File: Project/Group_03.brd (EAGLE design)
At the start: 56.4 x 71.1 mm, 29 parts, among them J1 POWER_JACKPTH_LOCK, U1 +12v, U3 TCA9546APW, U4 TMUX1208RSV

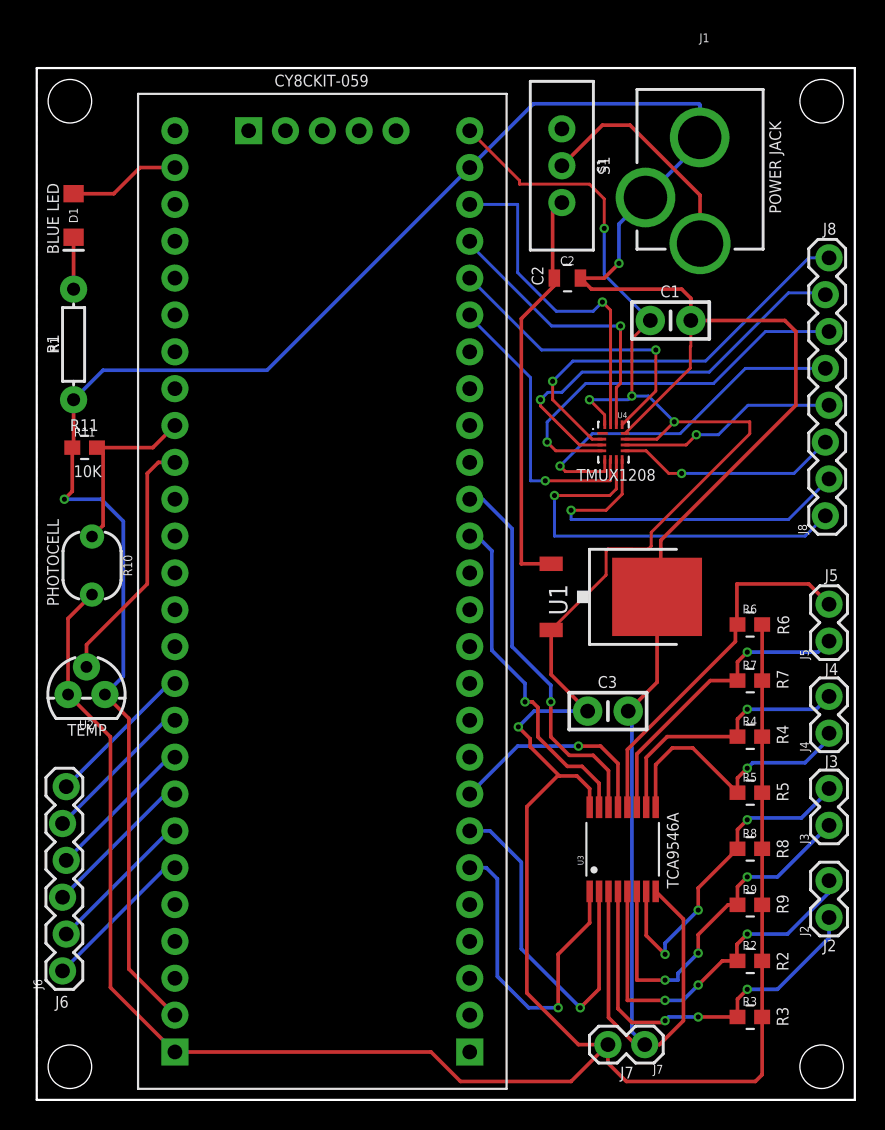
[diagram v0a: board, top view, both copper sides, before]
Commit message: Polygon isolation correction
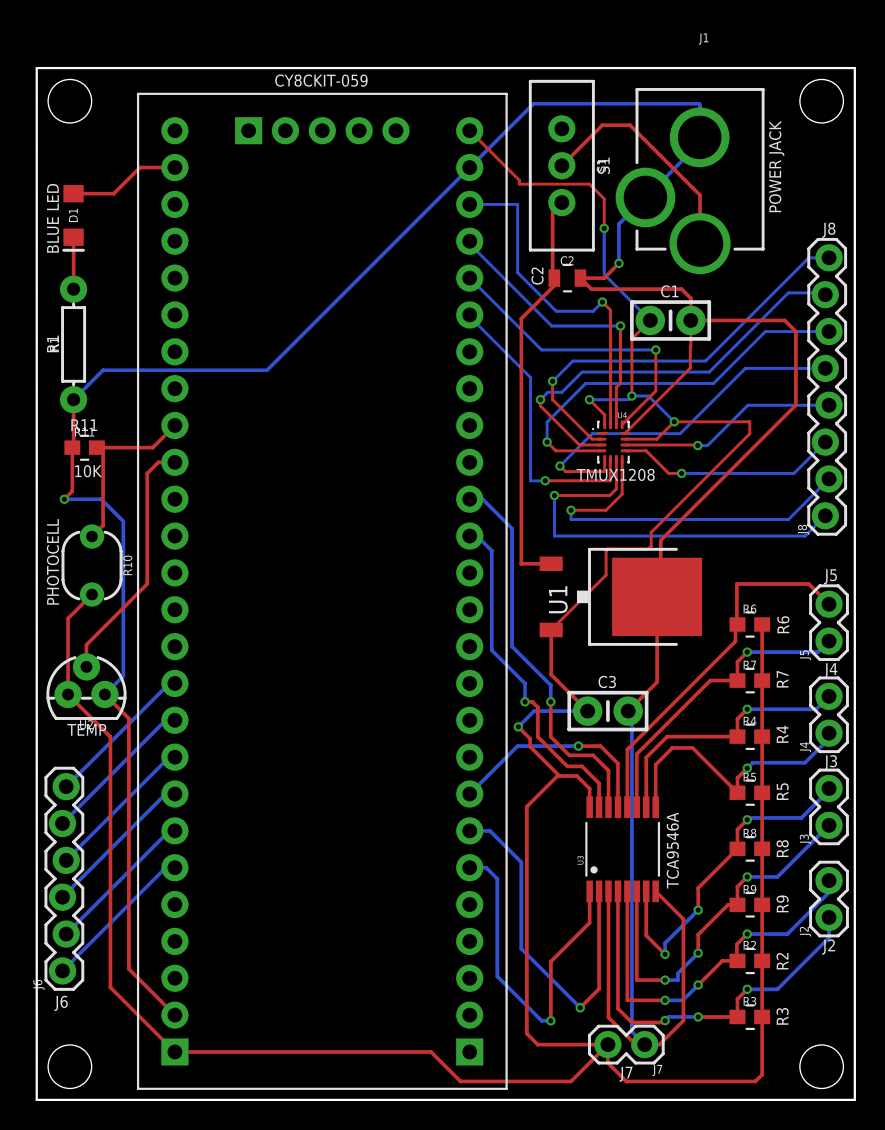
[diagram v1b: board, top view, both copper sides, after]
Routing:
- net 5V: track 220.2 -> 221.8 mm
- net I2C_A0: track 23.0 -> 23.9 mm
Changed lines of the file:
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@@
 <layer number="27" name="tValues" color="7" fill="1" visible="yes" active="yes"/>
 <layer number="28" name="bValues" color="7" fill="1" visible="yes" active="yes"/>
-<layer number="29" name="tStop" color="7" fill="3" visible="yes" active="yes"/>
+<layer number="29" name="tStop" color="7" fill="3" visible="no" active="yes"/>
 <layer number="30" name="bStop" color="7" fill="6" visible="no" active="yes"/>
 <layer number="31" name="tCream" color="7" fill="4" visible="no" active="yes"/>
@@
 <layer number="35" name="tGlue" color="7" fill="4" visible="no" active="yes"/>
 <layer number="36" name="bGlue" color="7" fill="5" visible="no" active="yes"/>
-<layer number="37" name="tTest" color="7" fill="1" visible="yes" active="yes"/>
-<layer number="38" name="bTest" color="7" fill="1" visible="yes" active="yes"/>
+<layer number="37" name="tTest" color="7" fill="1" visible="no" active="yes"/>
+<layer number="38" name="bTest" color="7" fill="1" visible="no" active="yes"/>
 <layer number="39" name="tKeepout" color="4" fill="11" visible="no" active="yes"/>
 <layer number="40" name="bKeepout" color="1" fill="11" visible="no" active="yes"/>
@@
 <layer number="49" name="Reference" color="7" fill="1" visible="yes" active="yes"/>
 <layer number="50" name="dxf" color="7" fill="1" visible="no" active="no"/>
-<layer number="51" name="tDocu" color="7" fill="1" visible="no" active="yes"/>
+<layer number="51" name="tDocu" color="7" fill="1" visible="yes" active="yes"/>
 <layer number="52" name="bDocu" color="7" fill="1" visible="yes" active="yes"/>
 <layer number="53" name="tGND_GNDA" color="7" fill="9" visible="no" active="no"/>
@@
 <text x="16.383" y="69.85" size="0.8128" layer="21" font="vector" ratio="24">CY8CKIT-059</text>
 <wire x1="3.048" y1="45.77" x2="3.556" y2="45.77" width="0.1524" layer="21"/>
-<wire x1="3.048" y1="44.173" x2="3.556" y2="44.173" width="0.1524" layer="21"/>
+<wire x1="3.048" y1="44.123" x2="3.556" y2="44.123" width="0.1524" layer="21"/>
 <wire x1="48.895" y1="33.601" x2="49.403" y2="33.601" width="0.1524" layer="21"/>
 <wire x1="48.915" y1="31.931" x2="49.423" y2="31.931" width="0.1524" layer="21"/>
@@
 <wire x1="34.0106" y1="24.8904" x2="33.193" y2="25.708" width="0.254" layer="1"/>
 <wire x1="38.111" y1="21.452" x2="37.2364" y2="22.3266" width="0.254" layer="1"/>
-<wire x1="39.37" y1="3.81" x2="37.338" y2="3.81" width="0.254" layer="1"/>
-<wire x1="37.338" y1="3.81" x2="33.782" y2="7.366" width="0.254" layer="1"/>
-<wire x1="33.782" y1="7.366" x2="33.782" y2="20.2089375" width="0.254" layer="1"/>
+<wire x1="39.37" y1="3.81" x2="34.538" y2="3.81" width="0.254" layer="1"/>
+<wire x1="34.538" y1="3.81" x2="33.782" y2="4.566" width="0.254" layer="1"/>
+<wire x1="33.782" y1="4.566" x2="33.782" y2="20.2089375" width="0.254" layer="1"/>
 <wire x1="33.782" y1="20.2089375" x2="35.8996625" y2="22.3266" width="0.254" layer="1"/>
 <wire x1="49.999" y1="32.765996875" x2="49.999" y2="28.90156875" width="0.254" layer="1"/>
@@
 <wire x1="37.973" y1="26.797" x2="35.459" y2="29.311" width="0.254" layer="1"/>
 <wire x1="39.243" y1="36.175" x2="35.459" y2="32.391" width="0.2032" layer="1"/>
-<polygon width="0.1524" layer="16" isolate="0.254">
+<polygon width="0.1524" layer="16" isolate="0.3048">
 <vertex x="0" y="0"/>
 <vertex x="56.388" y="0"/>
@@
 <wire x1="41.021" y1="26.543" x2="41.021" y2="4.699" width="0.254" layer="16"/>
 <wire x1="41.021" y1="4.699" x2="41.91" y2="3.81" width="0.254" layer="16"/>
-<polygon width="0.1524" layer="1" isolate="0.254">
+<polygon width="0.1524" layer="1" isolate="0.3048">
 <vertex x="0" y="0"/>
 <vertex x="56.388" y="0"/>
@@
 <contactref element="U$1" pad="6"/>
 <wire x1="38.111" y1="14.372" x2="38.111" y2="12.203" width="0.254" layer="1"/>
-<wire x1="38.111" y1="12.203" x2="35.941" y2="10.033" width="0.254" layer="1"/>
-<wire x1="35.941" y1="10.033" x2="35.941" y2="6.35" width="0.254" layer="1"/>
-<via x="35.941" y="6.35" extent="1-16" drill="0.35"/>
-<wire x1="35.941" y1="6.35" x2="33.909" y2="6.35" width="0.254" layer="16"/>
+<wire x1="38.111" y1="12.203" x2="35.441" y2="9.533" width="0.254" layer="1"/>
+<wire x1="35.441" y1="9.533" x2="35.441" y2="5.45" width="0.254" layer="1"/>
+<via x="35.441" y="5.45" extent="1-16" drill="0.35"/>
+<wire x1="35.441" y1="5.45" x2="34.809" y2="5.45" width="0.254" layer="16"/>
 <wire x1="31.75" y1="8.509" x2="31.75" y2="15.24" width="0.254" layer="16"/>
 <wire x1="31.75" y1="15.24" x2="30.988" y2="16.002" width="0.254" layer="16"/>
 <wire x1="30.988" y1="16.002" x2="29.845" y2="16.002" width="0.254" layer="16"/>
-<wire x1="33.909" y1="6.35" x2="31.75" y2="8.509" width="0.254" layer="16"/>
+<wire x1="34.809" y1="5.45" x2="31.75" y2="8.509" width="0.254" layer="16"/>
 </signal>
 <signal name="I2C_A1">
@@
 <contactref element="J8" pad="4"/>
 <contactref element="U4" pad="10"/>
-<wire x1="40.551" y1="45.139" x2="44.758" y2="45.139" width="0.2032" layer="1"/>
-<wire x1="44.758" y1="45.139" x2="45.466" y2="45.847" width="0.2032" layer="1"/>
-<via x="45.466" y="45.847" extent="1-16" drill="0.35"/>
-<wire x1="45.466" y1="45.847" x2="46.99" y2="45.847" width="0.2032" layer="16"/>
-<wire x1="46.99" y1="45.847" x2="49.022" y2="47.879" width="0.2032" layer="16"/>
+<wire x1="40.551" y1="45.139" x2="45.524" y2="45.139" width="0.2032" layer="1"/>
+<wire x1="45.524" y1="45.139" x2="45.566" y2="45.097" width="0.2032" layer="1"/>
+<via x="45.566" y="45.097" extent="1-16" drill="0.35"/>
+<wire x1="45.566" y1="45.097" x2="46.24" y2="45.097" width="0.2032" layer="16"/>
+<wire x1="46.24" y1="45.097" x2="49.022" y2="47.879" width="0.2032" layer="16"/>
 <wire x1="49.022" y1="47.879" x2="54.61" y2="47.879" width="0.2032" layer="16"/>
 </signal>

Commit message: Last modifications
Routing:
- net N$18: track 28.5 -> 29.9 mm
- net MUX_A0: track 23.9 -> 23.0 mm
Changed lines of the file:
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@@
 <contactref element="U4" pad="6"/>
 <wire x1="29.845" y1="54.102" x2="29.845" y2="53.975" width="0.2032" layer="16"/>
-<wire x1="29.845" y1="53.975" x2="34.036" y2="49.784" width="0.2032" layer="16"/>
-<wire x1="34.036" y1="49.784" x2="34.036" y2="42.672" width="0.2032" layer="16"/>
-<wire x1="34.036" y1="42.672" x2="35.052" y2="42.672" width="0.2032" layer="16"/>
+<wire x1="29.845" y1="53.975" x2="33.286" y2="50.534" width="0.2032" layer="16"/>
+<wire x1="33.286" y1="50.534" x2="33.286" y2="42.672" width="0.2032" layer="16"/>
+<wire x1="33.286" y1="42.672" x2="35.052" y2="42.672" width="0.2032" layer="16"/>
 <via x="35.052" y="42.672" extent="1-16" drill="0.35"/>
 <wire x1="39.5304" y1="42.672" x2="39.5304" y2="44.1184" width="0.2032" layer="1"/>
@@
 <contactref element="U$1" pad="24"/>
 <contactref element="U4" pad="15"/>
-<wire x1="35.814" y1="54.356" x2="33.147" y2="57.023" width="0.2032" layer="16"/>
-<wire x1="33.147" y1="57.023" x2="33.147" y2="61.722" width="0.2032" layer="16"/>
+<wire x1="35.76" y1="55.01" x2="33.147" y2="57.623" width="0.2032" layer="16"/>
+<wire x1="33.147" y1="57.623" x2="33.147" y2="61.722" width="0.2032" layer="16"/>
 <wire x1="33.147" y1="61.722" x2="29.845" y2="61.722" width="0.2032" layer="16"/>
 <wire x1="39.551" y1="46.539" x2="39.551" y2="54.429" width="0.2032" layer="1"/>
 <wire x1="39.551" y1="54.429" x2="38.989" y2="54.991" width="0.2032" layer="1"/>
 <via x="38.989" y="54.991" extent="1-16" drill="0.35"/>
-<wire x1="38.989" y1="54.991" x2="38.354" y2="54.356" width="0.2032" layer="16"/>
-<wire x1="38.354" y1="54.356" x2="35.814" y2="54.356" width="0.2032" layer="16"/>
+<wire x1="38.989" y1="54.991" x2="38.97" y2="55.01" width="0.2032" layer="16"/>
+<wire x1="38.97" y1="55.01" x2="35.76" y2="55.01" width="0.2032" layer="16"/>
 </signal>
 <signal name="N$2">
@@
 <contactref element="U4" pad="7"/>
 <wire x1="39.951" y1="44.139" x2="39.951" y2="42.11" width="0.2032" layer="1"/>
-<wire x1="39.497" y1="41.656" x2="35.687" y2="41.656" width="0.2032" layer="1"/>
-<via x="35.687" y="41.656" extent="1-16" drill="0.35"/>
-<wire x1="39.951" y1="42.11" x2="39.497" y2="41.656" width="0.2032" layer="1"/>
-<wire x1="35.687" y1="41.656" x2="35.687" y2="38.862" width="0.2032" layer="16"/>
-<wire x1="35.687" y1="38.862" x2="52.959" y2="38.862" width="0.2032" layer="16"/>
+<wire x1="39.447" y1="41.606" x2="34.987" y2="41.606" width="0.2032" layer="1"/>
+<via x="34.987" y="41.606" extent="1-16" drill="0.35"/>
+<wire x1="39.951" y1="42.11" x2="39.447" y2="41.606" width="0.2032" layer="1"/>
+<wire x1="34.987" y1="41.606" x2="34.987" y2="38.862" width="0.2032" layer="16"/>
+<wire x1="34.987" y1="38.862" x2="52.959" y2="38.862" width="0.2032" layer="16"/>
 <wire x1="52.959" y1="38.862" x2="54.356" y2="40.259" width="0.2032" layer="16"/>
 </signal>
